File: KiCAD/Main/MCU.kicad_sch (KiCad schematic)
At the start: 27 parts, among them Q4 2N7002, SW1 RESET, SW2 USER, U4 STM32H750VBTx, Y2 SiT8008xx-2x-xxE (25MHz)

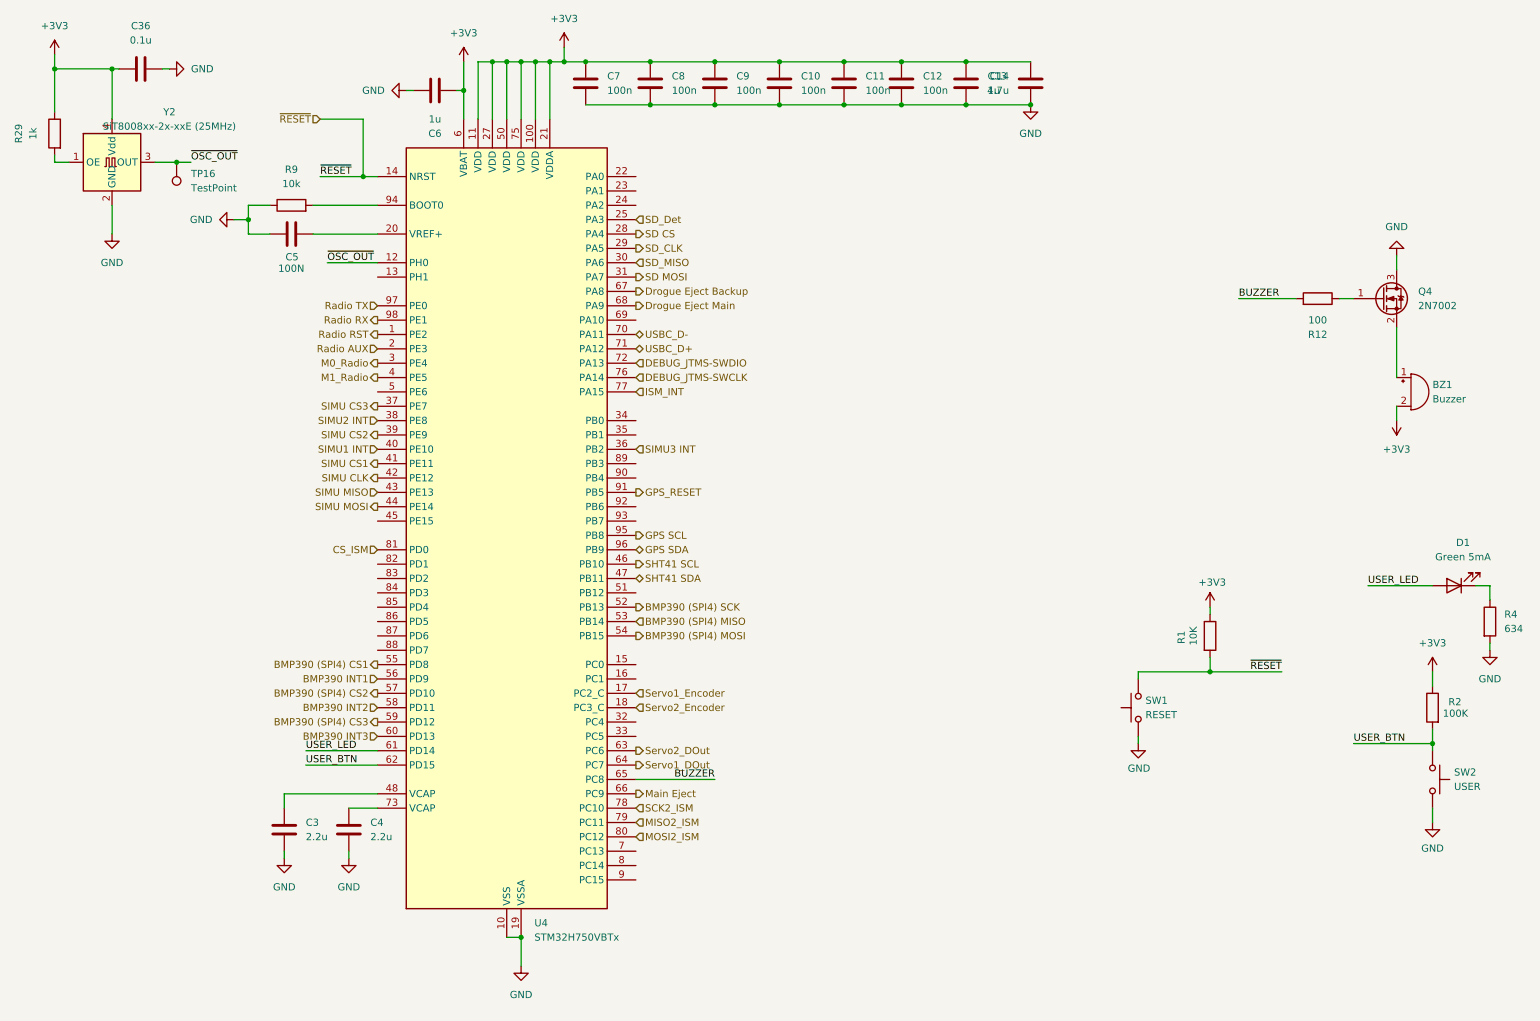
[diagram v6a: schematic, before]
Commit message: Replace independent magnetometer, reformat test points, generate test gerber and BOM
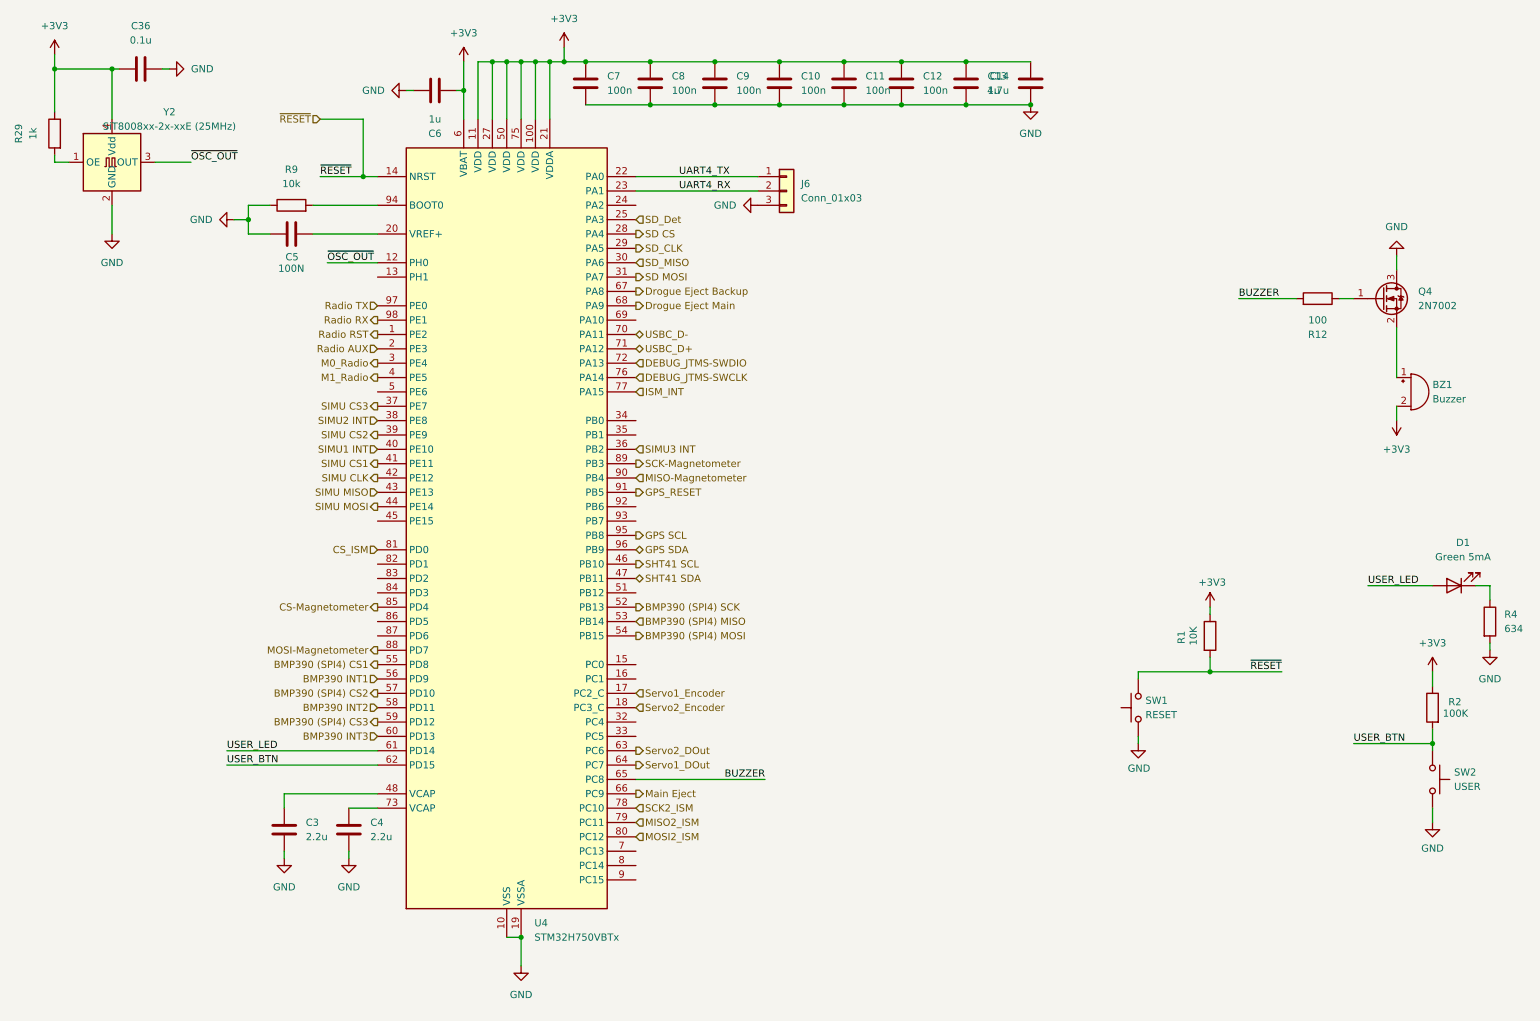
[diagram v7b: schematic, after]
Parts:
- removed TP16: TestPoint, TestPoint:TestPoint_THTPad_1.5x1.5mm_Drill0.7mm, symbol Connector:TestPoint
- added J6: Conn_01x03, Connector_PinHeader_2.54mm:PinHeader_1x03_P2.54mm_Vertical, symbol Connector_Generic:Conn_01x03
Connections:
- net GND: now also J6.3 (Pin_3)
- net UART4_TX: now reaches U4.22 (PA0)
- net UART4_TX: now also J6.1 (Pin_1)
- net UART4_RX: now reaches U4.23 (PA1)
- net UART4_RX: now also J6.2 (Pin_2)
- net CS-Magnetometer: now reaches U4.85 (PD4)
- net MOSI-Magnetometer: now reaches U4.88 (PD7)
- net SCK-Magnetometer: now reaches U4.89 (PB3)
- net MISO-Magnetometer: now reaches U4.90 (PB4)

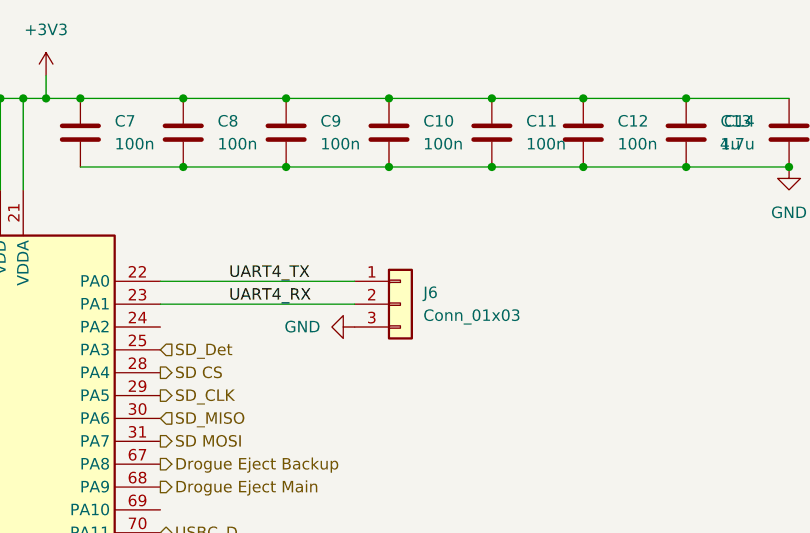
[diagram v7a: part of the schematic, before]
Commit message: Update BOM and respective components according to LCSC supply, remove previously generated production files
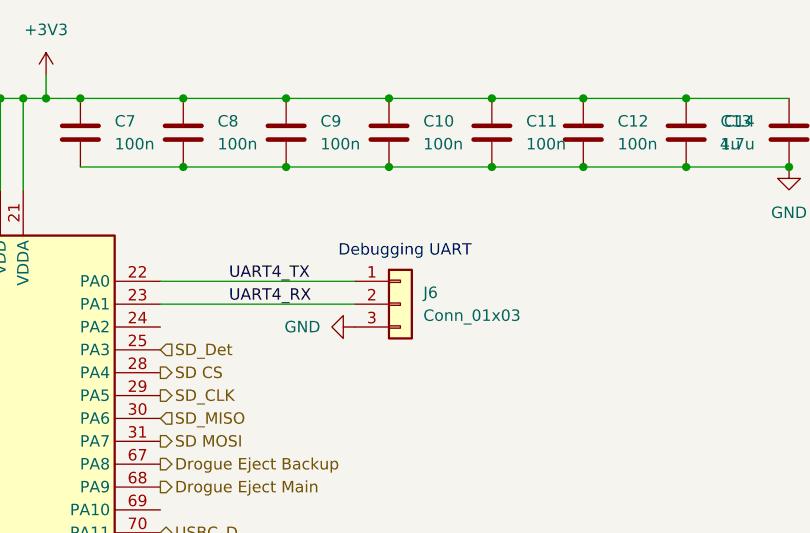
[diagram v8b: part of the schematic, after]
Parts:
- J6: now left out of the parts list
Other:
- note added: "Debugging UART"
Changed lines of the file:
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@@
 	(generator_version "9.0")
 	(paper "A4")
+	(text "Debugging UART"
+		(exclude_from_sim no)
+		(at 151.638 38.608 0)
+		(effects
+			(font
+				(size 1.27 1.27)
+			)
+		)
+	)
 	(junction
 		(at 104.14 21.59)
@@
 		(unit 1)
 		(exclude_from_sim no)
-		(in_bom yes)
+		(in_bom no)
 		(on_board yes)
 		(dnp no)
